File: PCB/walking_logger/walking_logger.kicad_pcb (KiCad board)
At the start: 2 copper layers, 116.8 x 60.2 mm, 7 parts, among them SW1 SW_SPDT

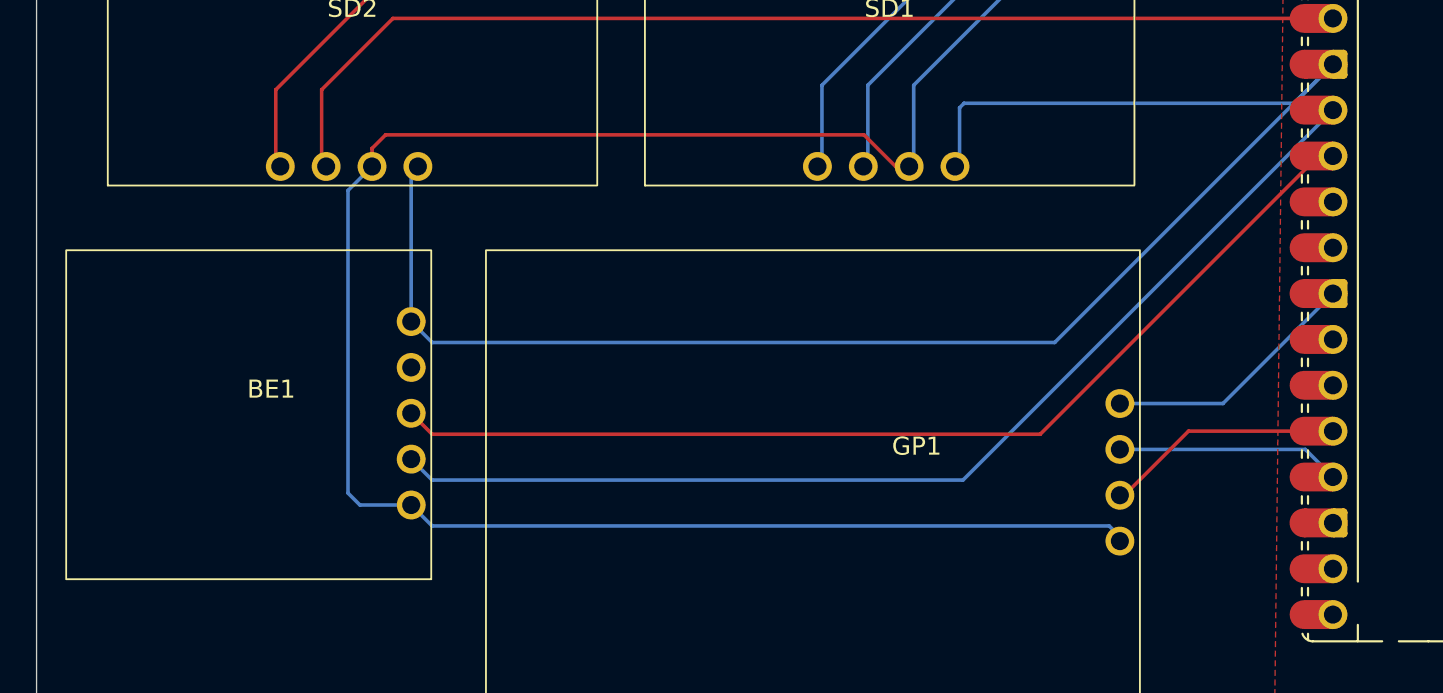
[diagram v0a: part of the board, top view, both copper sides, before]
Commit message: Added bill of materials and readme
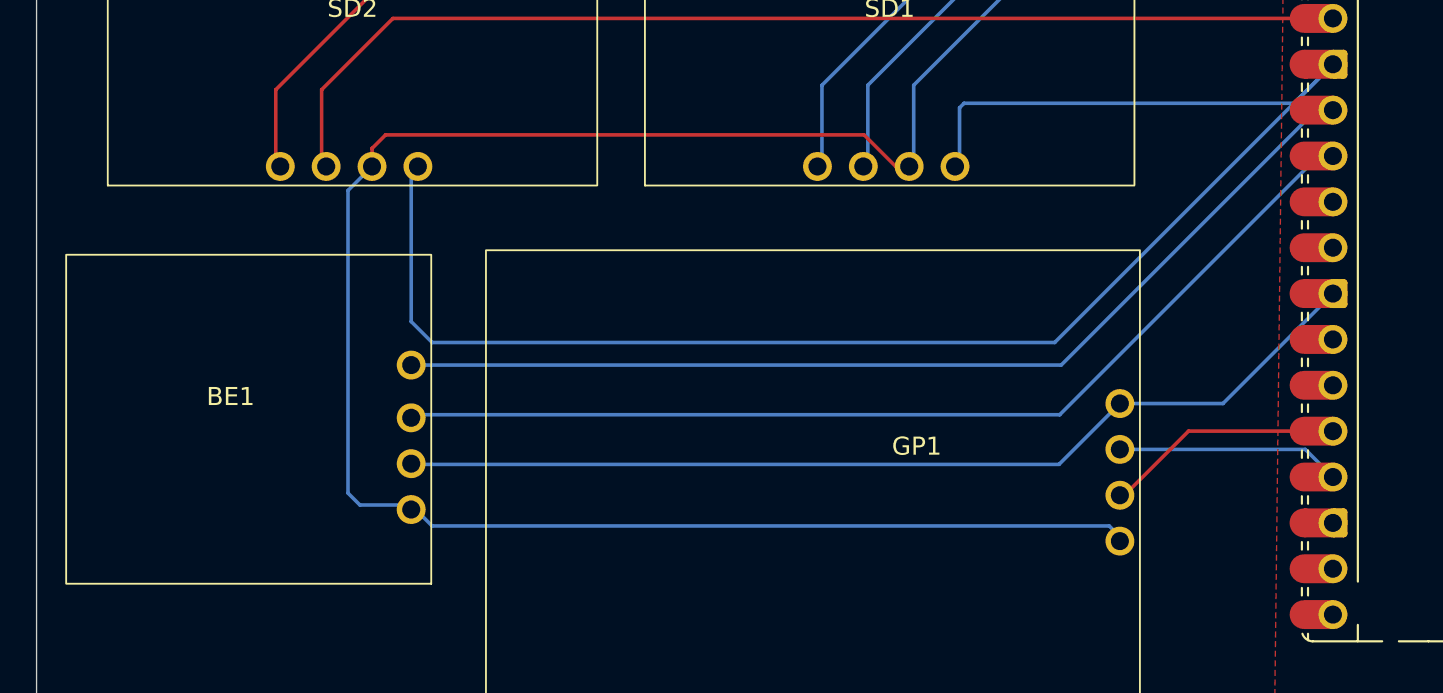
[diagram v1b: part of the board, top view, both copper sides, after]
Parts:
- moved BE1 0.25 mm to (110.5, 123.8)
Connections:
- BE1 pad 1: Net-(A1-GPIO6) -> GND
- BE1 pad 3: unconnected-(BE1-Pad3) -> Net-(A1-GPIO6)
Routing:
- net GND: track 125.7 -> 166.3 mm
- net Net-(A1-GPIO6): track 60.0 -> 56.9 mm
- net Net-(A1-GPIO7): track 57.1 -> 56.2 mm
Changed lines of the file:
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@@
 			(outputformat 1)
 			(mirror no)
-			(drillshape 1)
+			(drillshape 0)
 			(scaleselection 1)
-			(outputdirectory "")
+			(outputdirectory "../output/")
 		)
 	)
@@
 	(net 56 "unconnected-(A1-GPIO27_ADC1-Pad32)_1")
 	(net 57 "unconnected-(A1-GPIO14-Pad19)_1")
-	(net 58 "unconnected-(BE1-Pad3)")
-	(net 59 "Net-(BT1-+)")
-	(net 60 "unconnected-(SW1-C-Pad3)")
-	(net 61 "Net-(A1-GPIO7)")
+	(net 58 "Net-(BT1-+)")
+	(net 59 "unconnected-(SW1-C-Pad3)")
+	(net 60 "Net-(A1-GPIO7)")
+	(footprint "bme280:BME280"
+		(layer "F.Cu")
+		(at 110.5 123.75 180)
+		(tags "bme temp pressure humidity")
+		(property "Reference" "BE1"
+			(at 10 6.25 0)
+			(unlocked yes)
+			(layer "F.SilkS")
+			(effects
+				(font
+					(size 1 1)
+					(thickness 0.1)
+				)
+			)
+		)
+		(property "Value" "bme280"
+			(at 10 4.75 0)
+			(unlocked yes)
+			(layer "F.Fab")
+			(effects
+				(font
+					(size 1 1)
+					(thickness 0.15)
+				)
+			)
+		)
+		(property "Datasheet" ""
+			(at 0 0 180)
+			(unlocked yes)
+			(layer "F.Fab")
+			(hide yes)
+			(effects
+				(font
+					(size 1 1)
+					(thickness 0.15)
+				)
+			)
+		)
+		(property "Description" ""
+			(at 0 0 180)
+			(unlocked yes)
+			(layer "F.Fab")
+			(hide yes)
+			(effects
+				(font
+					(size 1 1)
+					(thickness 0.15)
+				)
+			)
+		)
+		(sheetname "/")
+		(sheetfile "walking_logger.kicad_sch")
+		(attr through_hole)
+		(fp_rect
+			(start -1.11 -4.11)
+			(end 19.11 14.11)
+			(stroke
+				(width 0.1)
+				(type solid)
+			)
+			(fill no)
+			(layer "F.SilkS")
+		)
+		(fp_rect
+			(start -1.5 -4.5)
+			(end 19.5 14.5)
+			(stroke
+				(width 0.1)
+				(type solid)
+			)
+			(fill no)
+			(layer "F.CrtYd")
+		)
+		(fp_rect
+			(start -1 -4)
+			(end 19 14)
+			(stroke
+				(width 0.1)
+				(type solid)
+			)
+			(fill no)
+			(layer "F.Fab")
+		)
+		(fp_text user "${REFERENCE}"
+			(at 10 3.25 0)
+			(unlocked yes)
+			(layer "F.Fab")
+			(effects
+				(font
+					(size 1 1)
+					(thickness 0.15)
+				)
+			)
+		)
+		(pad "0" thru_hole circle
+			(at 0 0 180)
+			(size 1.6 1.6)
+			(drill 1)
+			(layers "*.Cu" "*.Mask")
+			(remove_unused_layers no)
+			(net 6 "+3.3V")
+			(pinfunction "2-5V")
+			(pintype "power_in")
+		)
+		(pad "1" thru_hole circle
+			(at 0 2.54 180)
+			(size 1.6 1.6)
+			(drill 1)
+			(layers "*.Cu" "*.Mask")
+			(remove_unused_layers no)
+			(net 8 "GND")
+			(pinfunction "GND")
+			(pintype "power_in")
+		)
+		(pad "2" thru_hole circle
+			(at 0 5.08 180)
+			(size 1.6 1.6)
+			(drill 1)
+			(layers "*.Cu" "*.Mask")
+			(remove_unused_layers no)
+			(net 60 "Net-(A1-GPIO7)")
+			(pinfunction "SCL")
+			(pintype "bidirectional")
+		)
+		(pad "3" thru_hole circle
+			(at 0 8 180)
+			(size 1.6 1.6)
+			(drill 1)
+			(layers "*.Cu" "*.Mask")
+			(remove_unused_layers no)
+			(net 16 "Net-(A1-GPIO6)")
+			(pinfunction "SDA")
+			(pintype "bidirectional")
+		)
+		(embedded_fonts no)
+	)
 	(footprint "Button_Switch_THT:SW_Lever_1P2T_NKK_GW12LxH"
 		(layer "F.Cu")
@@
 			(layers "*.Cu" "*.Mask")
 			(remove_unused_layers no)
-			(net 59 "Net-(BT1-+)")
+			(net 58 "Net-(BT1-+)")
 			(pinfunction "B")
 			(pintype "passive")
@@
 			(layers "*.Cu" "*.Mask")
 			(remove_unused_layers no)
-			(net 60 "unconnected-(SW1-C-Pad3)")
+			(net 59 "unconnected-(SW1-C-Pad3)")
 			(pinfunction "C")
 			(pintype "passive+no_connect")
@@
 			(layers "F.Cu" "F.Mask")
 			(roundrect_rratio 0.5)
-			(net 61 "Net-(A1-GPIO7)")
+			(net 60 "Net-(A1-GPIO7)")
 			(pinfunction "GPIO7")
 			(pintype "bidirectional")
@@
 			(layers "*.Cu" "*.Mask")
 			(remove_unused_layers no)
-			(net 61 "Net-(A1-GPIO7)")
+			(net 60 "Net-(A1-GPIO7)")
 			(pinfunction "GPIO7")
 			(pintype "bidirectional")
@@
 		)
 	)
-	(footprint "bme280:BME280"
-		(layer "F.Cu")
-		(at 110.5 123.5 180)
-		(tags "bme temp pressure humidity")
-		(property "Reference" "BE1"
-			(at 7.75 6.41 0)
-			(unlocked yes)
-			(layer "F.SilkS")
-			(effects
-				(font
-					(size 1 1)
-					(thickness 0.1)
-				)
-			)
-		)
-		(property "Value" "bme280"
-			(at 7.75 4.91 0)
-			(unlocked yes)
-			(layer "F.Fab")
-			(effects
-				(font
-					(size 1 1)
-					(thickness 0.15)
-				)
-			)
-		)
-		(property "Datasheet" ""
-			(at 0 0 180)
-			(unlocked yes)
-			(layer "F.Fab")
-			(hide yes)
-			(effects
-				(font
-					(size 1 1)
-					(thickness 0.15)
-				)
-			)
-		)
-		(property "Description" ""
-			(at 0 0 180)
-			(unlocked yes)
-			(layer "F.Fab")
-			(hide yes)
-			(effects
-				(font
-					(size 1 1)
-					(thickness 0.15)
-				)
-			)
-		)
-		(sheetname "/")
-		(sheetfile "walking_logger.kicad_sch")
-		(attr through_hole)
-		(fp_rect
-			(start -1.11 -4.11)
-			(end 19.11 14.11)
-			(stroke
-				(width 0.1)
-				(type solid)
-			)
-			(fill no)
-			(layer "F.SilkS")
-		)
-		(fp_rect
-			(start -1.5 -4.5)
-			(end 19.5 14.5)
-			(stroke
-				(width 0.1)
-				(type solid)
-			)
-			(fill no)
-			(layer "F.CrtYd")
-		)
-		(fp_rect
-			(start -1 -4)
-			(end 19 14)
-			(stroke
-				(width 0.1)
-				(type solid)
-			)
-			(fill no)
-			(layer "F.Fab")
-		)
-		(fp_text user "${REFERENCE}"
-			(at 7.75 3.41 0)
-			(unlocked yes)
-			(layer "F.Fab")
-			(effects
-				(font
-					(size 1 1)
-					(thickness 0.15)
-				)
-			)
-		)
-		(pad "0" thru_hole circle
-			(at 0 0 180)
-			(size 1.6 1.6)
-			(drill 1)
-			(layers "*.Cu" "*.Mask")
-			(remove_unused_layers no)
-			(net 6 "+3.3V")
-			(pinfunction "2-5V")
-			(pintype "power_in")
-		)
-		(pad "1" thru_hole circle
-			(at 0 2.54 180)
-			(size 1.6 1.6)
-			(drill 1)
-			(layers "*.Cu" "*.Mask")
-			(remove_unused_layers no)
-			(net 16 "Net-(A1-GPIO6)")
-			(pinfunction "SDA")
-			(pintype "bidirectional")
-		)
-		(pad "2" thru_hole circle
-			(at 0 5.08 180)
-			(size 1.6 1.6)
-			(drill 1)
-			(layers "*.Cu" "*.Mask")
-			(remove_unused_layers no)
-			(net 61 "Net-(A1-GPIO7)")
-			(pinfunction "SCL")
-			(pintype "bidirectional")
-		)
-		(pad "3" thru_hole circle
-			(at 0 7.62 180)
-			(size 1.6 1.6)
-			(drill 1)
-			(layers "*.Cu" "*.Mask")
-			(remove_unused_layers no)
-			(net 58 "unconnected-(BE1-Pad3)")
-			(pintype "no_connect")
-		)
-		(pad "4" thru_hole circle
-			(at 0 10.16 180)
-			(size 1.6 1.6)
-			(drill 1)
-			(layers "*.Cu" "*.Mask")
-			(remove_unused_layers no)
-			(net 8 "GND")
-			(pinfunction "GND")
-			(pintype "power_in")
-		)
-		(embedded_fonts no)
-	)
 	(footprint "ssd1306:ssd1306"
 		(layer "F.Cu")
@@
 			(remove_unused_layers no)
 			(roundrect_rratio 0.1136363636)
-			(net 59 "Net-(BT1-+)")
+			(net 58 "Net-(BT1-+)")
 			(pinfunction "+")
 			(pintype "passive")
@@
 	)
 	(segment
+		(start 149.75 117.88)
+		(end 146.38 121.25)
+		(width 0.2)
+		(layer "B.Cu")
+		(net 8)
+	)
+	(segment
 		(start 140.87 101.5)
 		(end 141.12 101.25)
@@
 	)
 	(segment
+		(start 110.54 121.25)
+		(end 110.5 121.21)
+		(width 0.2)
+		(layer "B.Cu")
+		(net 8)
+	)
+	(segment
 		(start 110.5 113.34)
 		(end 111.66 114.5)
@@
 	)
 	(segment
+		(start 146.38 121.25)
+		(end 110.54 121.25)
+		(width 0.2)
+		(layer "B.Cu")
+		(net 8)
+	)
+	(segment
 		(start 133.25 104.5)
 		(end 133.25 100.25)
@@
 	)
 	(segment
-		(start 110.5 120.96)
-		(end 111.66 122.12)
+		(start 110.5 115.75)
+		(end 146.5 115.75)
 		(width 0.2)
 		(layer "B.Cu")
@@
 	)
 	(segment
-		(start 141.06 122.12)
+		(start 160.62 101.63)
 		(end 161.55 101.63)
 		(width 0.2)
@@
 	)
 	(segment
-		(start 111.66 122.12)
-		(end 141.06 122.12)
+		(start 146.5 115.75)
+		(end 160.62 101.63)
 		(width 0.2)
 		(layer "B.Cu")
@@
 		(width 0.2)
 		(layer "F.Cu")
-		(net 59)
+		(net 58)
 	)
 	(segment
@@
 		(width 0.2)
 		(layer "F.Cu")
-		(net 59)
+		(net 58)
 	)
 	(segment
@@
 		(width 0.2)
 		(layer "F.Cu")
-		(net 59)
+		(net 58)
 	)
 	(segment
@@
 		(width 0.2)
 		(layer "F.Cu")
-		(net 59)
+		(net 58)
 	)
 	(segment
@@
 		(width 0.2)
 		(layer "F.Cu")
-		(net 59)
+		(net 58)
 	)
 	(segment
 		(start 110.5 118.42)
-		(end 111.66 119.58)
+		(end 110.58 118.5)
 		(width 0.2)
 		(layer "F.Cu")
-		(net 61)
+		(net 60)
 	)
 	(segment
-		(start 145.34 119.58)
-		(end 160.75 104.17)
+		(start 110.58 118.5)
+		(end 146.42 118.5)
 		(width 0.2)
-		(layer "F.Cu")
-		(net 61)
+		(layer "B.Cu")
+		(net 60)
 	)
 	(segment
-		(start 111.66 119.58)
-		(end 145.34 119.58)
+		(start 146.42 118.5)
+		(end 160.75 104.17)
 		(width 0.2)
-		(layer "F.Cu")
-		(net 61)
+		(layer "B.Cu")
+		(net 60)
 	)
 	(zone
